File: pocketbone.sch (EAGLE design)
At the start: 41 parts, among them J1 USD_CONNECTOR, U1 24LC_32AT-I/OT, U2 OSD3358, U3 SN74LVC1G07_DCK_5, Y1 CM200C-32.768KAZF-UT, Y2 445C33D24M00000

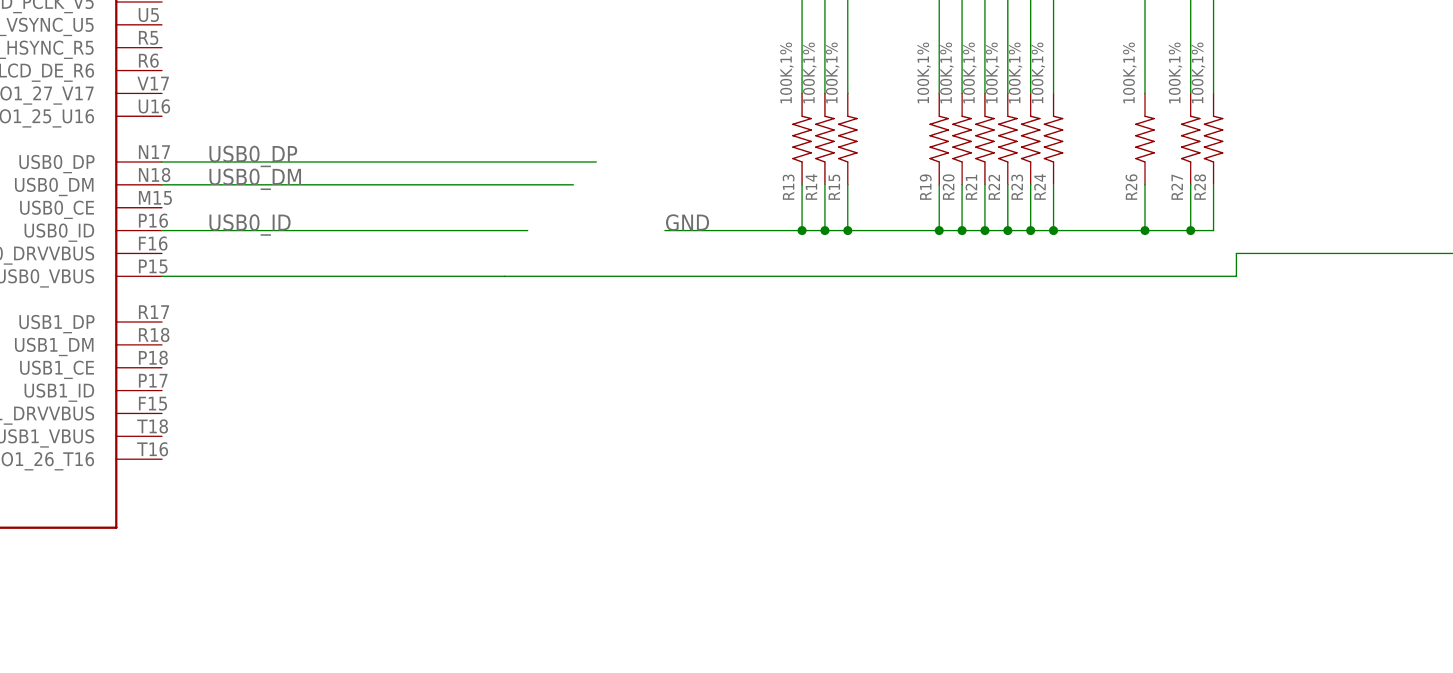
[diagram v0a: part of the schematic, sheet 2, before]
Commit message: Add the missing 2xµUSB OTG ports, cleanup
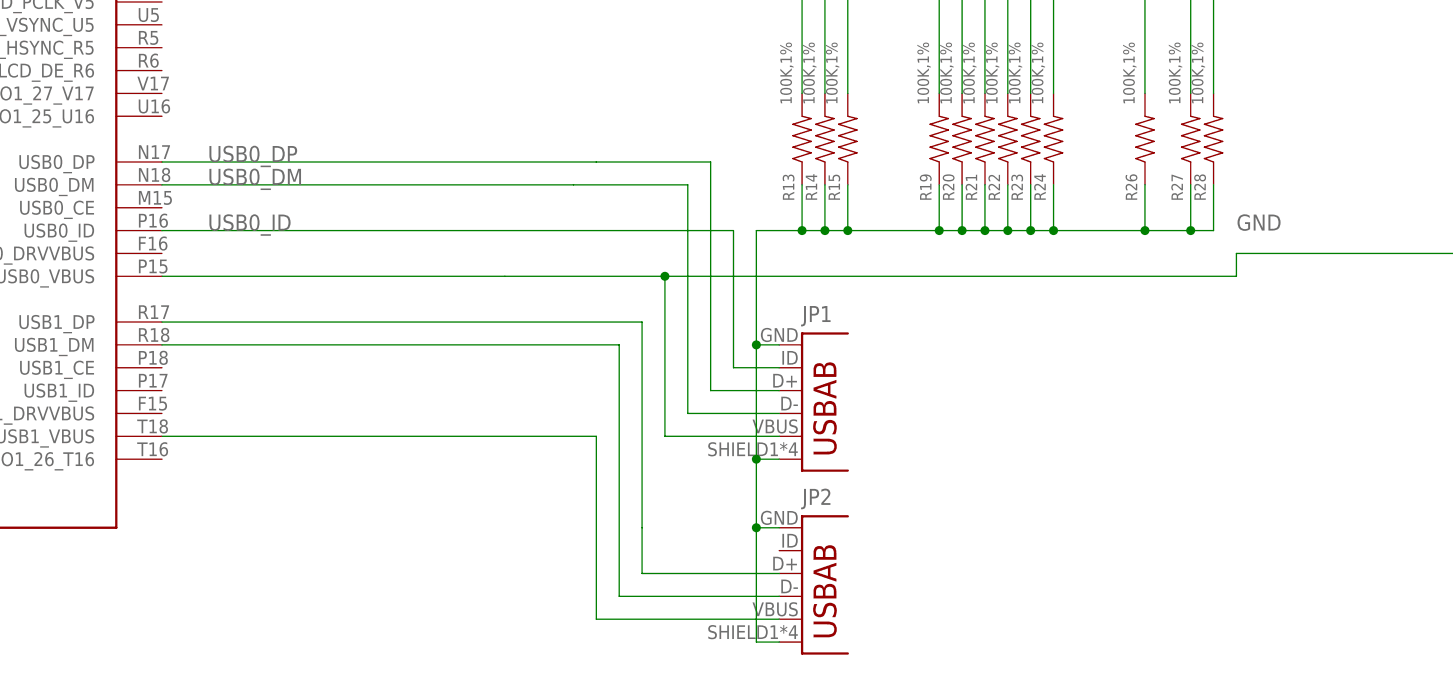
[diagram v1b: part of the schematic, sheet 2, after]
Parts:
- added JP1, JP2: (no value), pocketbone:USB-AB
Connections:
- new net N$1: JP2.D+, U2C.USB1_DP
- new net N$4: JP2.D-, U2C.USB1_DM
- new net N$6: JP2.VBUS, U2C.USB1_VBUS
- net GND: now also JP1.GND, JP1.SHIELD, JP2.GND, JP2.SHIELD
- net USB0_DM: now also JP1.D-
- net USB0_DP: now also JP1.D+
- net USB0_ID: now also JP1.USBID
- net USB_DC: now also JP1.VBUS
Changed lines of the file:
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@@
 <part name="POWER" library="SparkFun-Electromechanical" deviceset="SWITCH-MOMENTARY-2" device="SMD-1101NE"/>
 <part name="RESET" library="SparkFun-Electromechanical" deviceset="SWITCH-MOMENTARY-2" device="SMD-1101NE"/>
+<part name="JP1" library="pocketbone" deviceset="USB-AB" device=""/>
+<part name="JP2" library="pocketbone" deviceset="USB-AB" device=""/>
 </parts>
 <sheets>
@@
 <attribute name="VALUE" x="285.242" y="146.05" size="1.27" layer="96" rot="R90" align="center-left"/>
 </instance>
+<instance part="JP1" gate="G$1" x="264.16" y="114.3"/>
+<instance part="JP2" gate="G$1" x="264.16" y="93.98"/>
 </instances>
 <busses>
@@
 <pinref part="R13" gate="G$1" pin="1"/>
 <wire x1="261.62" y1="137.16" x2="261.62" y2="132.08" width="0.1524" layer="91"/>
-<wire x1="261.62" y1="132.08" x2="246.38" y2="132.08" width="0.1524" layer="91"/>
+<wire x1="261.62" y1="132.08" x2="256.54" y2="132.08" width="0.1524" layer="91"/>
 <pinref part="R14" gate="G$1" pin="1"/>
 <wire x1="261.62" y1="132.08" x2="264.16" y2="132.08" width="0.1524" layer="91"/>
@@
 <wire x1="289.56" y1="132.08" x2="299.72" y2="132.08" width="0.1524" layer="91"/>
 <wire x1="299.72" y1="132.08" x2="299.72" y2="137.16" width="0.1524" layer="91"/>
-<label x="246.38" y="132.08" size="1.778" layer="95"/>
+<label x="309.88" y="132.08" size="1.778" layer="95"/>
 <pinref part="R15" gate="G$1" pin="1"/>
 <wire x1="266.7" y1="137.16" x2="266.7" y2="132.08" width="0.1524" layer="91"/>
@@
 <wire x1="287.02" y1="132.08" x2="287.02" y2="137.16" width="0.1524" layer="91"/>
 <junction x="287.02" y="132.08"/>
+<pinref part="JP1" gate="G$1" pin="GND"/>
+<wire x1="259.08" y1="119.38" x2="256.54" y2="119.38" width="0.1524" layer="91"/>
+<wire x1="256.54" y1="119.38" x2="256.54" y2="132.08" width="0.1524" layer="91"/>
+<pinref part="JP1" gate="G$1" pin="SHIELD"/>
+<wire x1="259.08" y1="106.68" x2="256.54" y2="106.68" width="0.1524" layer="91"/>
+<wire x1="256.54" y1="106.68" x2="256.54" y2="119.38" width="0.1524" layer="91"/>
+<junction x="256.54" y="119.38"/>
+<wire x1="256.54" y1="106.68" x2="256.54" y2="99.06" width="0.1524" layer="91"/>
+<junction x="256.54" y="106.68"/>
+<pinref part="JP2" gate="G$1" pin="GND"/>
+<wire x1="256.54" y1="99.06" x2="259.08" y2="99.06" width="0.1524" layer="91"/>
+<wire x1="256.54" y1="99.06" x2="256.54" y2="86.36" width="0.1524" layer="91"/>
+<junction x="256.54" y="99.06"/>
+<pinref part="JP2" gate="G$1" pin="SHIELD"/>
+<wire x1="256.54" y1="86.36" x2="259.08" y2="86.36" width="0.1524" layer="91"/>
 </segment>
 </net>
@@
 <wire x1="190.5" y1="139.7" x2="238.76" y2="139.7" width="0.1524" layer="91"/>
 <label x="195.58" y="139.7" size="1.778" layer="95"/>
+<wire x1="238.76" y1="139.7" x2="251.46" y2="139.7" width="0.1524" layer="91"/>
+<wire x1="251.46" y1="139.7" x2="251.46" y2="114.3" width="0.1524" layer="91"/>
+<pinref part="JP1" gate="G$1" pin="D+"/>
+<wire x1="251.46" y1="114.3" x2="259.08" y2="114.3" width="0.1524" layer="91"/>
 </segment>
 </net>
@@
 <wire x1="190.5" y1="137.16" x2="236.22" y2="137.16" width="0.1524" layer="91"/>
 <label x="195.58" y="137.16" size="1.778" layer="95"/>
+<wire x1="236.22" y1="137.16" x2="248.92" y2="137.16" width="0.1524" layer="91"/>
+<wire x1="248.92" y1="137.16" x2="248.92" y2="111.76" width="0.1524" layer="91"/>
+<wire x1="248.92" y1="111.76" x2="259.08" y2="111.76" width="0.1524" layer="91"/>
+<pinref part="JP1" gate="G$1" pin="D-"/>
 </segment>
 </net>
@@
 <segment>
 <pinref part="U2" gate="C" pin="USB0_ID"/>
-<wire x1="190.5" y1="132.08" x2="231.14" y2="132.08" width="0.1524" layer="91"/>
+<wire x1="190.5" y1="132.08" x2="254" y2="132.08" width="0.1524" layer="91"/>
 <label x="195.58" y="132.08" size="1.778" layer="95"/>
+<wire x1="254" y1="132.08" x2="254" y2="116.84" width="0.1524" layer="91"/>
+<pinref part="JP1" gate="G$1" pin="USBID"/>
+<wire x1="254" y1="116.84" x2="259.08" y2="116.84" width="0.1524" layer="91"/>
 </segment>
 </net>
@@
 <wire x1="309.88" y1="127" x2="309.88" y2="129.54" width="0.1524" layer="91"/>
 <wire x1="190.5" y1="127" x2="228.6" y2="127" width="0.1524" layer="91"/>
-<wire x1="228.6" y1="127" x2="309.88" y2="127" width="0.1524" layer="91"/>
+<wire x1="228.6" y1="127" x2="246.38" y2="127" width="0.1524" layer="91"/>
 <pinref part="U2" gate="C" pin="USB0_VBUS"/>
 <label x="340.36" y="129.54" size="1.778" layer="95"/>
+<wire x1="246.38" y1="127" x2="309.88" y2="127" width="0.1524" layer="91"/>
 <wire x1="309.88" y1="129.54" x2="345.44" y2="129.54" width="0.1524" layer="91"/>
-</segment>
-</net>
+<wire x1="246.38" y1="127" x2="246.38" y2="109.22" width="0.1524" layer="91"/>
+<junction x="246.38" y="127"/>
+<pinref part="JP1" gate="G$1" pin="VBUS"/>
+<wire x1="246.38" y1="109.22" x2="259.08" y2="109.22" width="0.1524" layer="91"/>
+</segment>
+</net>
+<net name="N$1" class="0">
+<segment>
+<pinref part="U2" gate="C" pin="USB1_DP"/>
+<wire x1="190.5" y1="121.92" x2="243.84" y2="121.92" width="0.1524" layer="91"/>
+<wire x1="243.84" y1="121.92" x2="243.84" y2="99.06" width="0.1524" layer="91"/>
+<wire x1="243.84" y1="99.06" x2="243.84" y2="93.98" width="0.1524" layer="91"/>
+<pinref part="JP2" gate="G$1" pin="D+"/>
+<wire x1="243.84" y1="93.98" x2="259.08" y2="93.98" width="0.1524" layer="91"/>
+</segment>
+</net>
+<net name="N$4" class="0">
+<segment>
+<pinref part="U2" gate="C" pin="USB1_DM"/>
+<wire x1="190.5" y1="119.38" x2="241.3" y2="119.38" width="0.1524" layer="91"/>
+<wire x1="241.3" y1="119.38" x2="241.3" y2="91.44" width="0.1524" layer="91"/>
+<pinref part="JP2" gate="G$1" pin="D-"/>
+<wire x1="241.3" y1="91.44" x2="259.08" y2="91.44" width="0.1524" layer="91"/>
+</segment>
+</net>
+<net name="N$6" class="0">
+<segment>
+<pinref part="U2" gate="C" pin="USB1_VBUS"/>
+<wire x1="190.5" y1="109.22" x2="238.76" y2="109.22" width="0.1524" layer="91"/>
+<wire x1="238.76" y1="109.22" x2="238.76" y2="88.9" width="0.1524" layer="91"/>
+<pinref part="JP2" gate="G$1" pin="VBUS"/>
+<wire x1="238.76" y1="88.9" x2="259.08" y2="88.9" width="0.1524" layer="91"/>
+</segment>
+</net>

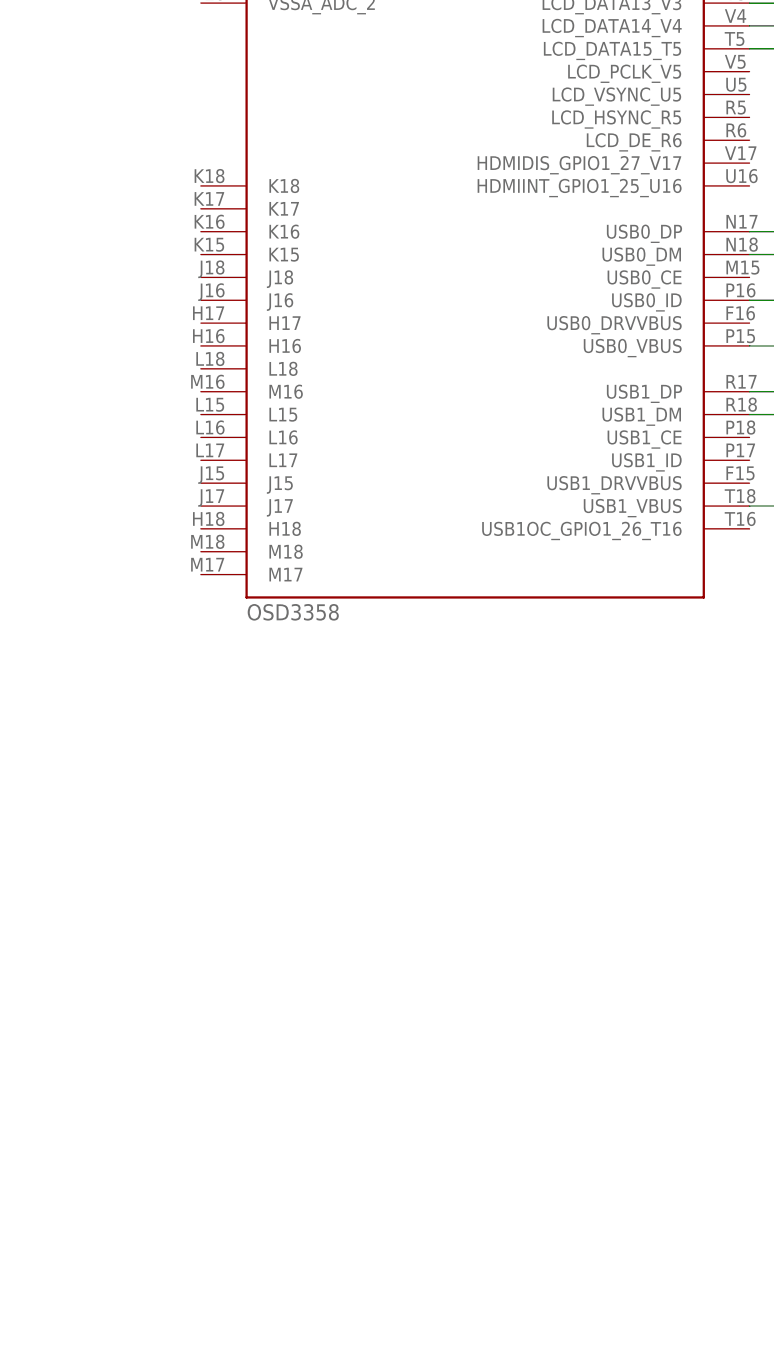
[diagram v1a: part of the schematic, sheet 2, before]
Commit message: Added AR8035 PHY (layout not done), reduced size
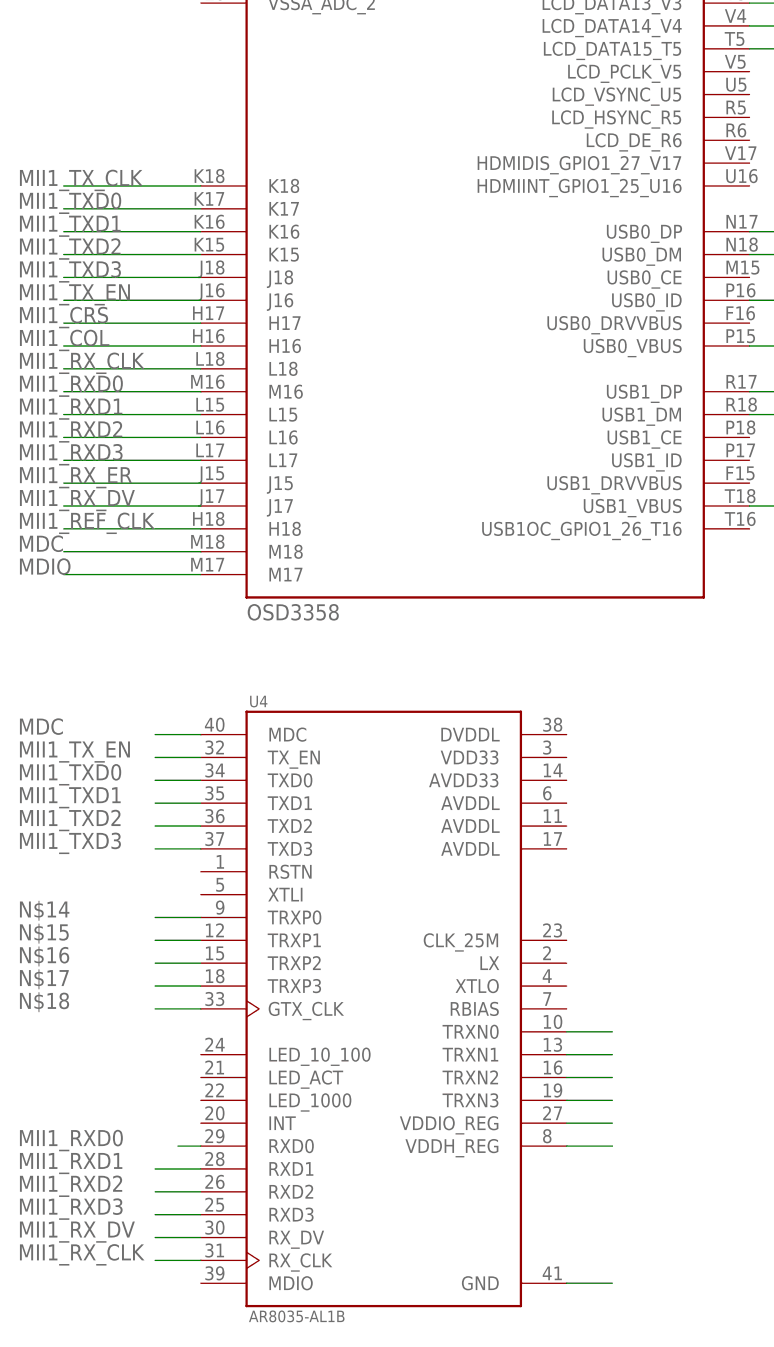
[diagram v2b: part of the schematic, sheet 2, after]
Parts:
- added U4: AR8035-AL1B, AR8035-AL1B:AR8035-AL1B
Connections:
- new net MDC: U2C.M18, U4.MDC
- new net MDIO: U2C.M17
- new net MII1_COL: U2C.H16
- new net MII1_CRS: U2C.H17
- new net MII1_REF_CLK: U2C.H18
- new net MII1_RXD0: U2C.M16, U4.RXD0
- new net MII1_RXD1: U2C.L15, U4.RXD1
- new net MII1_RXD2: U2C.L16, U4.RXD2
- new net MII1_RXD3: U2C.L17, U4.RXD3
- new net MII1_RX_CLK: U2C.L18, U4.RX_CLK
- new net MII1_RX_DV: U2C.J17, U4.RX_DV
- new net MII1_RX_ER: U2C.J15
- new net MII1_TXD0: U2C.K17, U4.TXD0
- new net MII1_TXD1: U2C.K16, U4.TXD1
- new net MII1_TXD2: U2C.K15, U4.TXD2
- new net MII1_TXD3: U2C.J18, U4.TXD3
- new net MII1_TX_CLK: U2C.K18
- new net MII1_TX_EN: U2C.J16, U4.TX_EN
- new net N$14: U4.TRXP0
- new net N$15: U4.TRXP1
- new net N$16: U4.TRXP2
- new net N$17: U4.TRXP3
- new net N$18: U4.GTX_CLK
- new net N$19: U4.TRXN0
- new net N$20: U4.TRXN1
- new net N$21: U4.TRXN2
- new net N$22: U4.TRXN3
- new net N$23: U4.VDDIO_REG
- new net N$24: U4.VDDH_REG
- new net N$7: U4.GND
